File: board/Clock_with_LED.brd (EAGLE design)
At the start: 50 x 50 mm, 18 parts

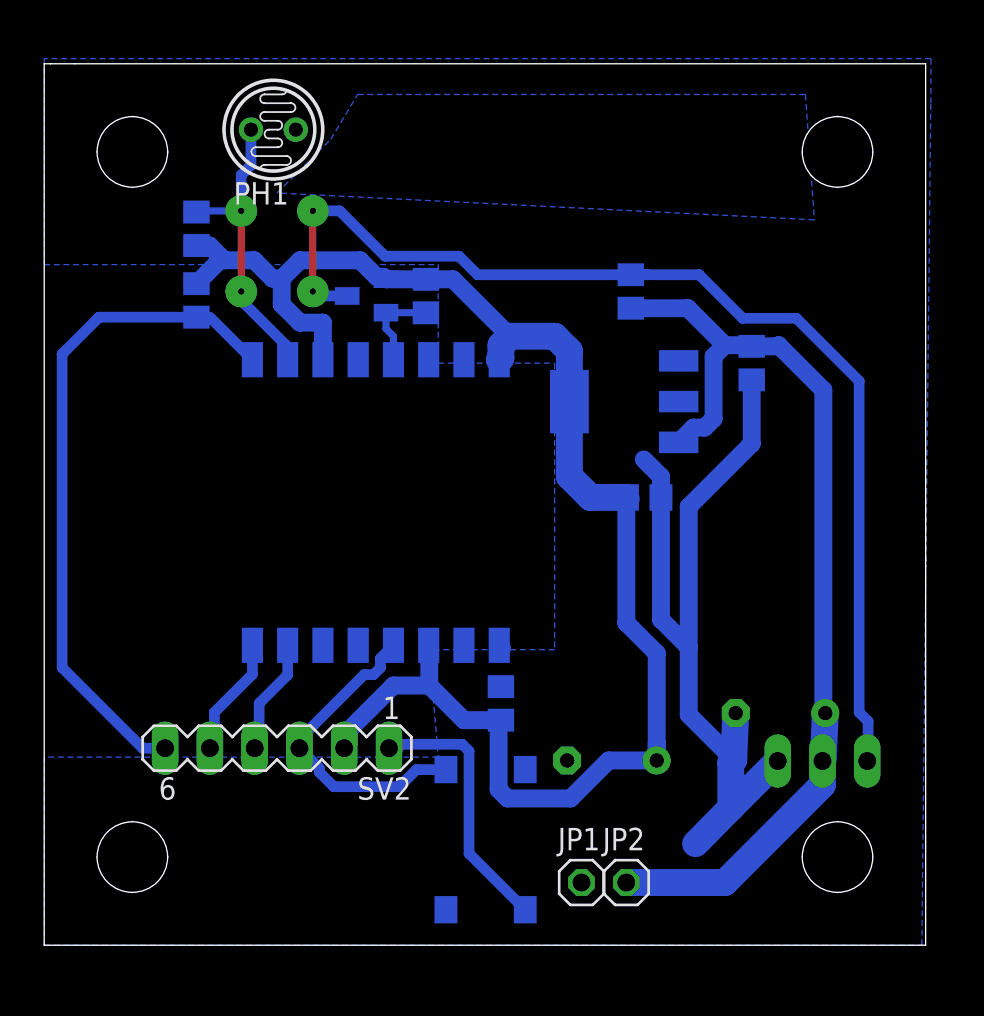
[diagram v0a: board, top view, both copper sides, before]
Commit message: Removed LEDs, organised PCB files
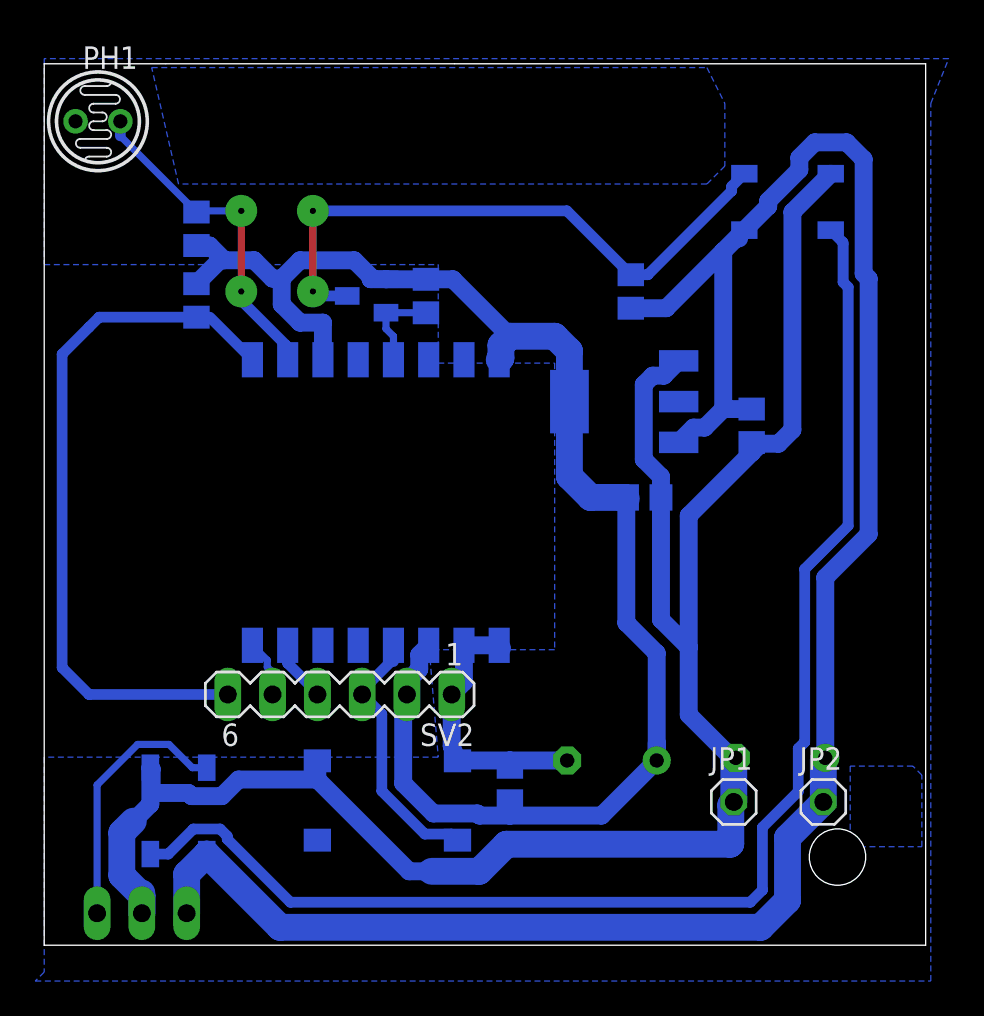
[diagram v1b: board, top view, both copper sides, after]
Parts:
- added D1, D2: WS2812B, WS2812B:LED_WS2812B
- moved SV1 39.6 mm to (5.54, 1.81)
- moved JP2 12.1 mm to (44.2, 8.13)
- moved PH1 9.96 mm to (3.05, 46.7), turned to 180 degrees
- moved JP1 9.77 mm to (39.1, 8.13)
- moved S1 6.00 mm to (19.5, 8.21), turned to 180 degrees
- moved SV2 4.68 mm to (16.8, 14.2)
- moved C5 4.60 mm to (26.4, 9.14)
- moved C3 3.56 mm to (40.1, 29.5)
- moved C1 2.54 mm to (41.8, 10.6)
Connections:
- new net N$1: D1.2, D2.4
- new net N$2: D1.4, SV1.1
- net +5V: now also D1.1, D2.1, SV1.3; no longer SV1.2
- net GND: now also D1.3, D2.3, SV1.2; no longer SV1.1
- net N$7: now also D2.2; no longer SV1.3
- net PRG_EN: now also S1.2; no longer S1.1
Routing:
- net N$1: track 8.00 -> 108.3 mm, vias 1 -> 0
- net GND: track 63.2 -> 127.5 mm
- net +5V: track 55.8 -> 115.3 mm
- net N$7: track 64.7 -> 35.5 mm
- net N$5: track 8.00 -> 0.00 mm, vias 1 -> 0
- net N$4: track 8.00 -> 0.00 mm
- net N$2: track 8.00 -> 15.0 mm, vias 1 -> 0
- net TXD: track 6.84 -> 3.26 mm
- net RXD: track 6.61 -> 3.49 mm
- net REST: track 42.2 -> 44.5 mm
- net ADC: track 16.9 -> 19.0 mm
- net VCC: track 90.1 -> 88.0 mm
- net PRG_EN: track 18.1 -> 16.1 mm
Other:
- outline, holes or cut-outs redrawn
- board text added: "-"
- board text added: "5V"
